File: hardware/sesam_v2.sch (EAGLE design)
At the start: 11 parts, among them X2 C-GRID-06-70543

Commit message: little changes
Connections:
- new net N$22: U$1.IN+, X1-1.KL
- net GND: no longer U$1.IN+, X1-1.KL
- net N$21: now also OLED.2
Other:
- moved on the sheet: OLED
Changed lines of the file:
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@@
 <instance part="RELAIS_3" gate="G$1" x="142.24" y="88.9"/>
 <instance part="SERIAL" gate="G$1" x="12.7" y="27.94"/>
-<instance part="OLED" gate="1" x="180.34" y="50.8" rot="R180"/>
+<instance part="OLED" gate="1" x="208.28" y="50.8" rot="R180"/>
 <instance part="X1" gate="-1" x="-38.1" y="71.12"/>
 <instance part="X1" gate="-2" x="-38.1" y="66.04"/>
@@
 <wire x1="55.88" y1="30.48" x2="55.88" y2="45.72" width="0.1524" layer="91"/>
 <pinref part="OLED" gate="1" pin="3"/>
-<wire x1="172.72" y1="50.8" x2="160.02" y2="50.8" width="0.1524" layer="91"/>
+<wire x1="200.66" y1="50.8" x2="160.02" y2="50.8" width="0.1524" layer="91"/>
 <wire x1="160.02" y1="50.8" x2="160.02" y2="20.32" width="0.1524" layer="91"/>
 <wire x1="160.02" y1="20.32" x2="160.02" y2="15.24" width="0.1524" layer="91"/>
@@
 <wire x1="0" y1="10.16" x2="45.72" y2="10.16" width="0.1524" layer="91"/>
 <pinref part="OLED" gate="1" pin="4"/>
-<wire x1="172.72" y1="48.26" x2="167.64" y2="48.26" width="0.1524" layer="91"/>
+<wire x1="200.66" y1="48.26" x2="167.64" y2="48.26" width="0.1524" layer="91"/>
 <wire x1="167.64" y1="48.26" x2="167.64" y2="45.72" width="0.1524" layer="91"/>
 <pinref part="D1" gate="1" pin="A"/>
@@
 <pinref part="X1" gate="-2" pin="KL"/>
 </segment>
-<segment>
-<pinref part="U$1" gate="G$1" pin="IN+"/>
-<wire x1="-27.94" y1="73.66" x2="-33.02" y2="73.66" width="0.1524" layer="91"/>
-<wire x1="-33.02" y1="73.66" x2="-33.02" y2="71.12" width="0.1524" layer="91"/>
-<pinref part="X1" gate="-1" pin="KL"/>
-</segment>
 </net>
 <net name="N$13" class="0">
@@
 <wire x1="127" y1="50.8" x2="132.08" y2="50.8" width="0.1524" layer="91"/>
 <wire x1="132.08" y1="50.8" x2="132.08" y2="53.34" width="0.1524" layer="91"/>
-<wire x1="132.08" y1="53.34" x2="175.26" y2="53.34" width="0.1524" layer="91"/>
+<wire x1="200.66" y1="53.34" x2="132.08" y2="53.34" width="0.1524" layer="91"/>
+<pinref part="OLED" gate="1" pin="2"/>
 </segment>
 </net>
@@
 <wire x1="-5.08" y1="27.94" x2="5.08" y2="27.94" width="0.1524" layer="91"/>
 <pinref part="OLED" gate="1" pin="1"/>
-<wire x1="172.72" y1="55.88" x2="129.54" y2="55.88" width="0.1524" layer="91"/>
+<wire x1="200.66" y1="55.88" x2="129.54" y2="55.88" width="0.1524" layer="91"/>
 <wire x1="129.54" y1="55.88" x2="129.54" y2="53.34" width="0.1524" layer="91"/>
 </segment>
@@
 </segment>
 </net>
+<net name="N$22" class="0">
+<segment>
+<pinref part="U$1" gate="G$1" pin="IN+"/>
+<wire x1="-27.94" y1="73.66" x2="-33.02" y2="73.66" width="0.1524" layer="91"/>
+<wire x1="-33.02" y1="73.66" x2="-33.02" y2="71.12" width="0.1524" layer="91"/>
+<pinref part="X1" gate="-1" pin="KL"/>
+</segment>
+</net>

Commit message: new nice layout
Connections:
- net N$12: now also U1.ADC; no longer U1.*GPIO9
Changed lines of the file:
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@@
-</segment>
-</net>
-<net name="N$12" class="0">
-<segment>
-<pinref part="U1" gate="G$1" pin="*GPIO9"/>
-<wire x1="99.06" y1="27.94" x2="99.06" y2="17.78" width="0.1524" layer="91"/>
-<wire x1="99.06" y1="17.78" x2="157.48" y2="17.78" width="0.1524" layer="91"/>
-<wire x1="157.48" y1="17.78" x2="157.48" y2="22.86" width="0.1524" layer="91"/>
-<pinref part="X2" gate="-4" pin="S"/>
-<wire x1="157.48" y1="22.86" x2="172.72" y2="22.86" width="0.1524" layer="91"/>
 </segment>
 </net>
@@
 </segment>
 </net>
+<net name="N$12" class="0">
+<segment>
+<wire x1="78.74" y1="12.7" x2="165.1" y2="12.7" width="0.1524" layer="91"/>
+<wire x1="165.1" y1="12.7" x2="165.1" y2="22.86" width="0.1524" layer="91"/>
+<wire x1="165.1" y1="22.86" x2="172.72" y2="22.86" width="0.1524" layer="91"/>
+<pinref part="X2" gate="-4" pin="S"/>
+<wire x1="172.72" y1="22.86" x2="175.26" y2="22.86" width="0.1524" layer="91"/>
+<junction x="172.72" y="22.86"/>
+<wire x1="78.74" y1="12.7" x2="78.74" y2="60.96" width="0.1524" layer="91"/>
+<pinref part="U1" gate="G$1" pin="ADC"/>
+<wire x1="83.82" y1="60.96" x2="78.74" y2="60.96" width="0.1524" layer="91"/>
+</segment>
+</net>

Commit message: ready for first board
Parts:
- RELAIS_1: value (none) -> V23100-V4005-A010
- RELAIS_2, RELAIS_3: value (none) -> V23100-A4005-A010
- renumbered U$1 to DC/DC, X1 to POWER, X2 to GPIO
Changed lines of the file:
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@@
 <parts>
 <part name="U1" library="esp8266modules" deviceset="ESP12E" device="SMD"/>
-<part name="U$1" library="diy-modules" deviceset="DC-DC-STEP-DOWN-LM2596" device=""/>
+<part name="DC/DC" library="diy-modules" deviceset="DC-DC-STEP-DOWN-LM2596" device=""/>
 <part name="OUTPUT_CON" library="con-molex" deviceset="C-GRID-06" device="-70543"/>
-<part name="RELAIS_1" library="ic-package" deviceset="DIL14" device="S"/>
-<part name="RELAIS_2" library="ic-package" deviceset="DIL14" device="S"/>
-<part name="RELAIS_3" library="ic-package" deviceset="DIL14" device="S"/>
+<part name="RELAIS_1" library="ic-package" deviceset="DIL14" device="S" value="V23100-V4005-A010"/>
+<part name="RELAIS_2" library="ic-package" deviceset="DIL14" device="S" value="V23100-A4005-A010"/>
+<part name="RELAIS_3" library="ic-package" deviceset="DIL14" device="S" value="V23100-A4005-A010"/>
 <part name="SERIAL" library="con-lstb" deviceset="MA04-2" device=""/>
 <part name="OLED" library="con-lstb" deviceset="MA04-1" device=""/>
-<part name="X1" library="con-wago-508" deviceset="W237-02P" device=""/>
+<part name="POWER" library="con-wago-508" deviceset="W237-02P" device=""/>
 <part name="D1" library="diode" deviceset="ZTE" device="" value="3.3V"/>
-<part name="X2" library="con-molex" deviceset="C-GRID-06" device="-70543"/>
+<part name="GPIO" library="con-molex" deviceset="C-GRID-06" device="-70543"/>
 </parts>
 <sheets>
@@
 <instances>
 <instance part="U1" gate="G$1" x="101.6" y="55.88"/>
-<instance part="U$1" gate="G$1" x="-10.16" y="68.58"/>
+<instance part="DC/DC" gate="G$1" x="-10.16" y="68.58"/>
 <instance part="OUTPUT_CON" gate="-1" x="170.18" y="78.74"/>
 <instance part="OUTPUT_CON" gate="-2" x="170.18" y="76.2"/>
@@
 <instance part="SERIAL" gate="G$1" x="12.7" y="27.94"/>
 <instance part="OLED" gate="1" x="208.28" y="50.8" rot="R180"/>
-<instance part="X1" gate="-1" x="-38.1" y="71.12"/>
-<instance part="X1" gate="-2" x="-38.1" y="66.04"/>
+<instance part="POWER" gate="-1" x="-38.1" y="71.12"/>
+<instance part="POWER" gate="-2" x="-38.1" y="66.04"/>
 <instance part="D1" gate="1" x="22.86" y="68.58" rot="R90"/>
-<instance part="X2" gate="-1" x="175.26" y="30.48"/>
-<instance part="X2" gate="-2" x="175.26" y="27.94"/>
-<instance part="X2" gate="-3" x="175.26" y="25.4"/>
-<instance part="X2" gate="-4" x="175.26" y="22.86"/>
-<instance part="X2" gate="-5" x="175.26" y="20.32"/>
-<instance part="X2" gate="-6" x="175.26" y="17.78"/>
+<instance part="GPIO" gate="-1" x="175.26" y="30.48"/>
+<instance part="GPIO" gate="-2" x="175.26" y="27.94"/>
+<instance part="GPIO" gate="-3" x="175.26" y="25.4"/>
+<instance part="GPIO" gate="-4" x="175.26" y="22.86"/>
+<instance part="GPIO" gate="-5" x="175.26" y="20.32"/>
+<instance part="GPIO" gate="-6" x="175.26" y="17.78"/>
 </instances>
 <busses>
@@
 <net name="3V3" class="0">
 <segment>
-<pinref part="U$1" gate="G$1" pin="OUT+"/>
+<pinref part="DC/DC" gate="G$1" pin="OUT+"/>
 <wire x1="7.62" y1="73.66" x2="22.86" y2="73.66" width="0.1524" layer="91"/>
 <wire x1="22.86" y1="73.66" x2="48.26" y2="73.66" width="0.1524" layer="91"/>
@@
 <pinref part="D1" gate="1" pin="C"/>
 <wire x1="22.86" y1="71.12" x2="22.86" y2="73.66" width="0.1524" layer="91"/>
-<pinref part="X2" gate="-5" pin="S"/>
+<pinref part="GPIO" gate="-5" pin="S"/>
 <wire x1="172.72" y1="20.32" x2="160.02" y2="20.32" width="0.1524" layer="91"/>
 <label x="17.78" y="78.74" size="1.778" layer="95"/>
@@
 <pinref part="RELAIS_3" gate="G$1" pin="9"/>
 <wire x1="154.94" y1="83.82" x2="149.86" y2="83.82" width="0.1524" layer="91"/>
-<pinref part="U$1" gate="G$1" pin="OUT-"/>
+<pinref part="DC/DC" gate="G$1" pin="OUT-"/>
 <wire x1="7.62" y1="63.5" x2="22.86" y2="63.5" width="0.1524" layer="91"/>
 <wire x1="22.86" y1="63.5" x2="45.72" y2="63.5" width="0.1524" layer="91"/>
@@
 <pinref part="D1" gate="1" pin="A"/>
 <wire x1="22.86" y1="66.04" x2="22.86" y2="63.5" width="0.1524" layer="91"/>
-<pinref part="X2" gate="-6" pin="S"/>
+<pinref part="GPIO" gate="-6" pin="S"/>
 <wire x1="172.72" y1="17.78" x2="167.64" y2="17.78" width="0.1524" layer="91"/>
 <label x="10.16" y="60.96" size="1.778" layer="95"/>
@@
 </segment>
 <segment>
-<pinref part="U$1" gate="G$1" pin="IN-"/>
+<pinref part="DC/DC" gate="G$1" pin="IN-"/>
 <wire x1="-33.02" y1="66.04" x2="-27.94" y2="66.04" width="0.1524" layer="91"/>
 <wire x1="-27.94" y1="66.04" x2="-27.94" y2="63.5" width="0.1524" layer="91"/>
-<pinref part="X1" gate="-2" pin="KL"/>
+<pinref part="POWER" gate="-2" pin="KL"/>
 </segment>
 </net>
@@
 <wire x1="116.84" y1="58.42" x2="147.32" y2="58.42" width="0.1524" layer="91"/>
 <wire x1="147.32" y1="58.42" x2="147.32" y2="30.48" width="0.1524" layer="91"/>
-<pinref part="X2" gate="-1" pin="S"/>
+<pinref part="GPIO" gate="-1" pin="S"/>
 <wire x1="147.32" y1="30.48" x2="172.72" y2="30.48" width="0.1524" layer="91"/>
 </segment>
@@
 <net name="N$10" class="0">
 <segment>
-<pinref part="X2" gate="-2" pin="S"/>
+<pinref part="GPIO" gate="-2" pin="S"/>
 <wire x1="172.72" y1="27.94" x2="124.46" y2="27.94" width="0.1524" layer="91"/>
 <wire x1="124.46" y1="27.94" x2="124.46" y2="55.88" width="0.1524" layer="91"/>
@@
 <wire x1="121.92" y1="20.32" x2="154.94" y2="20.32" width="0.1524" layer="91"/>
 <wire x1="154.94" y1="20.32" x2="154.94" y2="25.4" width="0.1524" layer="91"/>
-<pinref part="X2" gate="-3" pin="S"/>
+<pinref part="GPIO" gate="-3" pin="S"/>
 <wire x1="154.94" y1="25.4" x2="172.72" y2="25.4" width="0.1524" layer="91"/>
 </segment>
@@
 <net name="N$22" class="0">
 <segment>
-<pinref part="U$1" gate="G$1" pin="IN+"/>
+<pinref part="DC/DC" gate="G$1" pin="IN+"/>
 <wire x1="-27.94" y1="73.66" x2="-33.02" y2="73.66" width="0.1524" layer="91"/>
 <wire x1="-33.02" y1="73.66" x2="-33.02" y2="71.12" width="0.1524" layer="91"/>
-<pinref part="X1" gate="-1" pin="KL"/>
+<pinref part="POWER" gate="-1" pin="KL"/>
 </segment>
 </net>
@@
 <wire x1="165.1" y1="12.7" x2="165.1" y2="22.86" width="0.1524" layer="91"/>
 <wire x1="165.1" y1="22.86" x2="172.72" y2="22.86" width="0.1524" layer="91"/>
-<pinref part="X2" gate="-4" pin="S"/>
+<pinref part="GPIO" gate="-4" pin="S"/>
 <wire x1="172.72" y1="22.86" x2="175.26" y2="22.86" width="0.1524" layer="91"/>
 <junction x="172.72" y="22.86"/>

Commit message: nice new layout and board, better power supply added
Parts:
- removed D1: 3.3V, diode:ZTE
- added C1: 0.1µF, rcl:C-EUC0805
- added C2: 10µF, rcl:CPOL-EUE2-5
- added IC1: 337T, linear:337T
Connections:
- net N$10 renamed GPIO5
- net N$12 renamed ADC
- net N$13 renamed GPIO13
- net N$14 renamed GPIO12
- net N$15 renamed GPIO14
- net N$17 renamed TX
- net N$19 renamed RST
- net N$20 renamed RX
- net N$9 renamed GPIO4
- removed net N$11: GPIO-3.S, U1.GPIO15
- removed net N$16: OLED.1, SERIAL.6, U1.GPIO0
- removed net N$18: SERIAL.3, U1.GPIO16
- removed net N$21: OLED.2, SERIAL.4, U1.GPIO2
- new net GPIO0: OLED.1, SERIAL.4, U1.GPIO0
- new net GPIO15: GPIO-3.S, SERIAL.6, U1.GPIO15
- new net GPIO16: U1.GPIO16
- new net GPIO2: OLED.2, SERIAL.3, U1.GPIO2
- new net POWER: C1.1, DC/DC.OUT+, IC1.VO
- net 3V3: now also C2.+, IC1.VI, U1.CH_PD; no longer D1.C, DC/DC.OUT+
- net GND: now also C1.2, C2.-, IC1.ADJ; no longer D1.A
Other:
- moved on the sheet: OLED, RELAIS_3, U1

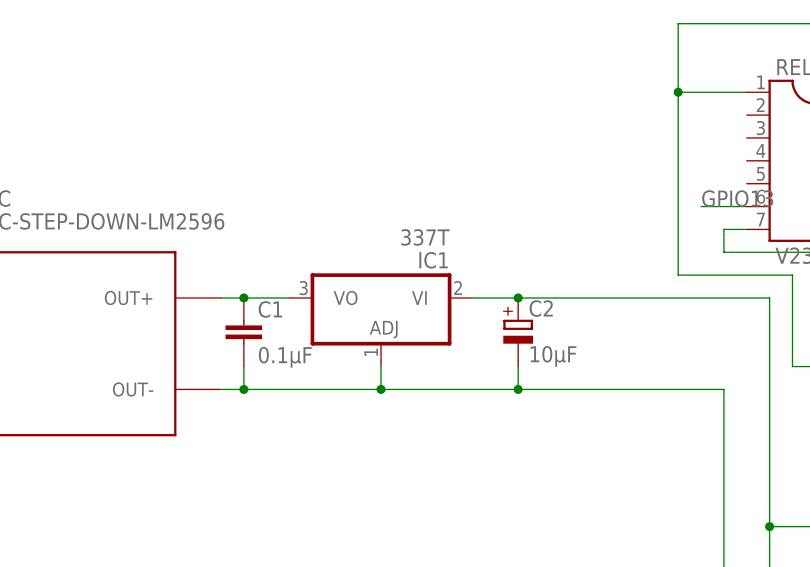
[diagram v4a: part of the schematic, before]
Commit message: fixed power regulator
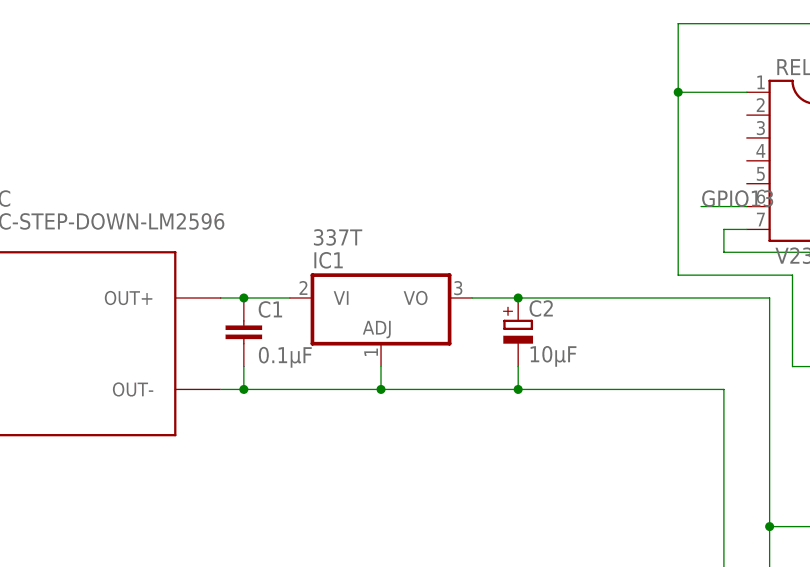
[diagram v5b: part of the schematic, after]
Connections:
- net 3V3: now also IC1.VO; no longer IC1.VI
- net POWER: now also IC1.VI; no longer IC1.VO
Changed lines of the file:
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@@
 <instance part="GPIO" gate="-5" x="175.26" y="20.32"/>
 <instance part="GPIO" gate="-6" x="175.26" y="17.78"/>
-<instance part="IC1" gate="A1" x="25.4" y="73.66" rot="R180"/>
+<instance part="IC1" gate="A1" x="25.4" y="73.66" rot="MR180"/>
 <instance part="C1" gate="G$1" x="10.16" y="71.12"/>
 <instance part="C2" gate="G$1" x="40.64" y="71.12"/>
@@
 <pinref part="C1" gate="G$1" pin="1"/>
 <wire x1="7.62" y1="73.66" x2="10.16" y2="73.66" width="0.1524" layer="91"/>
-<pinref part="IC1" gate="A1" pin="VO"/>
+<pinref part="IC1" gate="A1" pin="VI"/>
 <wire x1="10.16" y1="73.66" x2="15.24" y2="73.66" width="0.1524" layer="91"/>
 <junction x="10.16" y="73.66"/>
@@
 <net name="3V3" class="0">
 <segment>
-<pinref part="IC1" gate="A1" pin="VI"/>
 <pinref part="C2" gate="G$1" pin="+"/>
-<wire x1="35.56" y1="73.66" x2="40.64" y2="73.66" width="0.1524" layer="91"/>
 <wire x1="40.64" y1="73.66" x2="68.58" y2="73.66" width="0.1524" layer="91"/>
 <wire x1="68.58" y1="73.66" x2="68.58" y2="48.26" width="0.1524" layer="91"/>
-<junction x="40.64" y="73.66"/>
 <pinref part="U1" gate="G$1" pin="VCC"/>
 <wire x1="68.58" y1="48.26" x2="68.58" y2="35.56" width="0.1524" layer="91"/>
@@
 <junction x="68.58" y="48.26"/>
 <label x="76.2" y="48.26" size="1.778" layer="95"/>
+<pinref part="IC1" gate="A1" pin="VO"/>
+<wire x1="40.64" y1="73.66" x2="35.56" y2="73.66" width="0.1524" layer="91"/>
+<junction x="40.64" y="73.66"/>
 </segment>
 <segment>

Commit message: some layout tweeks
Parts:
- renumbered OUTPUT_CON to RELAYS_CON
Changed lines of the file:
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@@
 <part name="U1" library="esp8266modules" deviceset="ESP12E" device="SMD"/>
 <part name="DC/DC" library="diy-modules" deviceset="DC-DC-STEP-DOWN-LM2596" device=""/>
-<part name="OUTPUT_CON" library="con-molex" deviceset="C-GRID-06" device="-70543"/>
+<part name="RELAYS_CON" library="con-molex" deviceset="C-GRID-06" device="-70543"/>
 <part name="RELAIS_1" library="ic-package" deviceset="DIL14" device="S" value="V23100-V4005-A010"/>
 <part name="RELAIS_2" library="ic-package" deviceset="DIL14" device="S" value="V23100-A4005-A010"/>
@@
 <instance part="U1" gate="G$1" x="101.6" y="45.72"/>
 <instance part="DC/DC" gate="G$1" x="-10.16" y="68.58"/>
-<instance part="OUTPUT_CON" gate="-1" x="170.18" y="78.74"/>
-<instance part="OUTPUT_CON" gate="-2" x="170.18" y="76.2"/>
-<instance part="OUTPUT_CON" gate="-3" x="170.18" y="73.66"/>
-<instance part="OUTPUT_CON" gate="-4" x="170.18" y="71.12"/>
-<instance part="OUTPUT_CON" gate="-5" x="170.18" y="68.58"/>
-<instance part="OUTPUT_CON" gate="-6" x="170.18" y="66.04"/>
+<instance part="RELAYS_CON" gate="-1" x="170.18" y="78.74"/>
+<instance part="RELAYS_CON" gate="-2" x="170.18" y="76.2"/>
+<instance part="RELAYS_CON" gate="-3" x="170.18" y="73.66"/>
+<instance part="RELAYS_CON" gate="-4" x="170.18" y="71.12"/>
+<instance part="RELAYS_CON" gate="-5" x="170.18" y="68.58"/>
+<instance part="RELAYS_CON" gate="-6" x="170.18" y="66.04"/>
 <instance part="RELAIS_1" gate="G$1" x="73.66" y="88.9"/>
 <instance part="RELAIS_2" gate="G$1" x="104.14" y="88.9"/>
@@
 <wire x1="149.86" y1="101.6" x2="124.46" y2="101.6" width="0.1524" layer="91"/>
 <wire x1="124.46" y1="101.6" x2="124.46" y2="96.52" width="0.1524" layer="91"/>
-<pinref part="OUTPUT_CON" gate="-2" pin="S"/>
+<pinref part="RELAYS_CON" gate="-2" pin="S"/>
 <wire x1="124.46" y1="96.52" x2="124.46" y2="76.2" width="0.1524" layer="91"/>
 <wire x1="124.46" y1="76.2" x2="167.64" y2="76.2" width="0.1524" layer="91"/>
@@
 <wire x1="129.54" y1="78.74" x2="147.32" y2="78.74" width="0.1524" layer="91"/>
 <wire x1="147.32" y1="78.74" x2="147.32" y2="81.28" width="0.1524" layer="91"/>
-<pinref part="OUTPUT_CON" gate="-1" pin="S"/>
+<pinref part="RELAYS_CON" gate="-1" pin="S"/>
 <wire x1="147.32" y1="81.28" x2="167.64" y2="81.28" width="0.1524" layer="91"/>
 <wire x1="167.64" y1="81.28" x2="167.64" y2="78.74" width="0.1524" layer="91"/>
@@
 <wire x1="96.52" y1="96.52" x2="88.9" y2="96.52" width="0.1524" layer="91"/>
 <junction x="88.9" y="96.52"/>
-<pinref part="OUTPUT_CON" gate="-4" pin="S"/>
+<pinref part="RELAYS_CON" gate="-4" pin="S"/>
 <wire x1="167.64" y1="71.12" x2="88.9" y2="71.12" width="0.1524" layer="91"/>
 </segment>
@@
 <net name="N$13" class="0">
 <segment>
-<pinref part="OUTPUT_CON" gate="-3" pin="S"/>
+<pinref part="RELAYS_CON" gate="-3" pin="S"/>
 <pinref part="RELAIS_2" gate="G$1" pin="8"/>
 <wire x1="167.64" y1="73.66" x2="111.76" y2="73.66" width="0.1524" layer="91"/>
@@
 <net name="N$14" class="0">
 <segment>
-<pinref part="OUTPUT_CON" gate="-6" pin="S"/>
+<pinref part="RELAYS_CON" gate="-6" pin="S"/>
 <wire x1="167.64" y1="66.04" x2="71.12" y2="66.04" width="0.1524" layer="91"/>
 <wire x1="71.12" y1="66.04" x2="71.12" y2="76.2" width="0.1524" layer="91"/>
@@
 <wire x1="83.82" y1="78.74" x2="83.82" y2="68.58" width="0.1524" layer="91"/>
 <junction x="83.82" y="78.74"/>
-<pinref part="OUTPUT_CON" gate="-5" pin="S"/>
+<pinref part="RELAYS_CON" gate="-5" pin="S"/>
 <wire x1="83.82" y1="68.58" x2="167.64" y2="68.58" width="0.1524" layer="91"/>
 </segment>
